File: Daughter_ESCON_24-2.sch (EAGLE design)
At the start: 29 parts

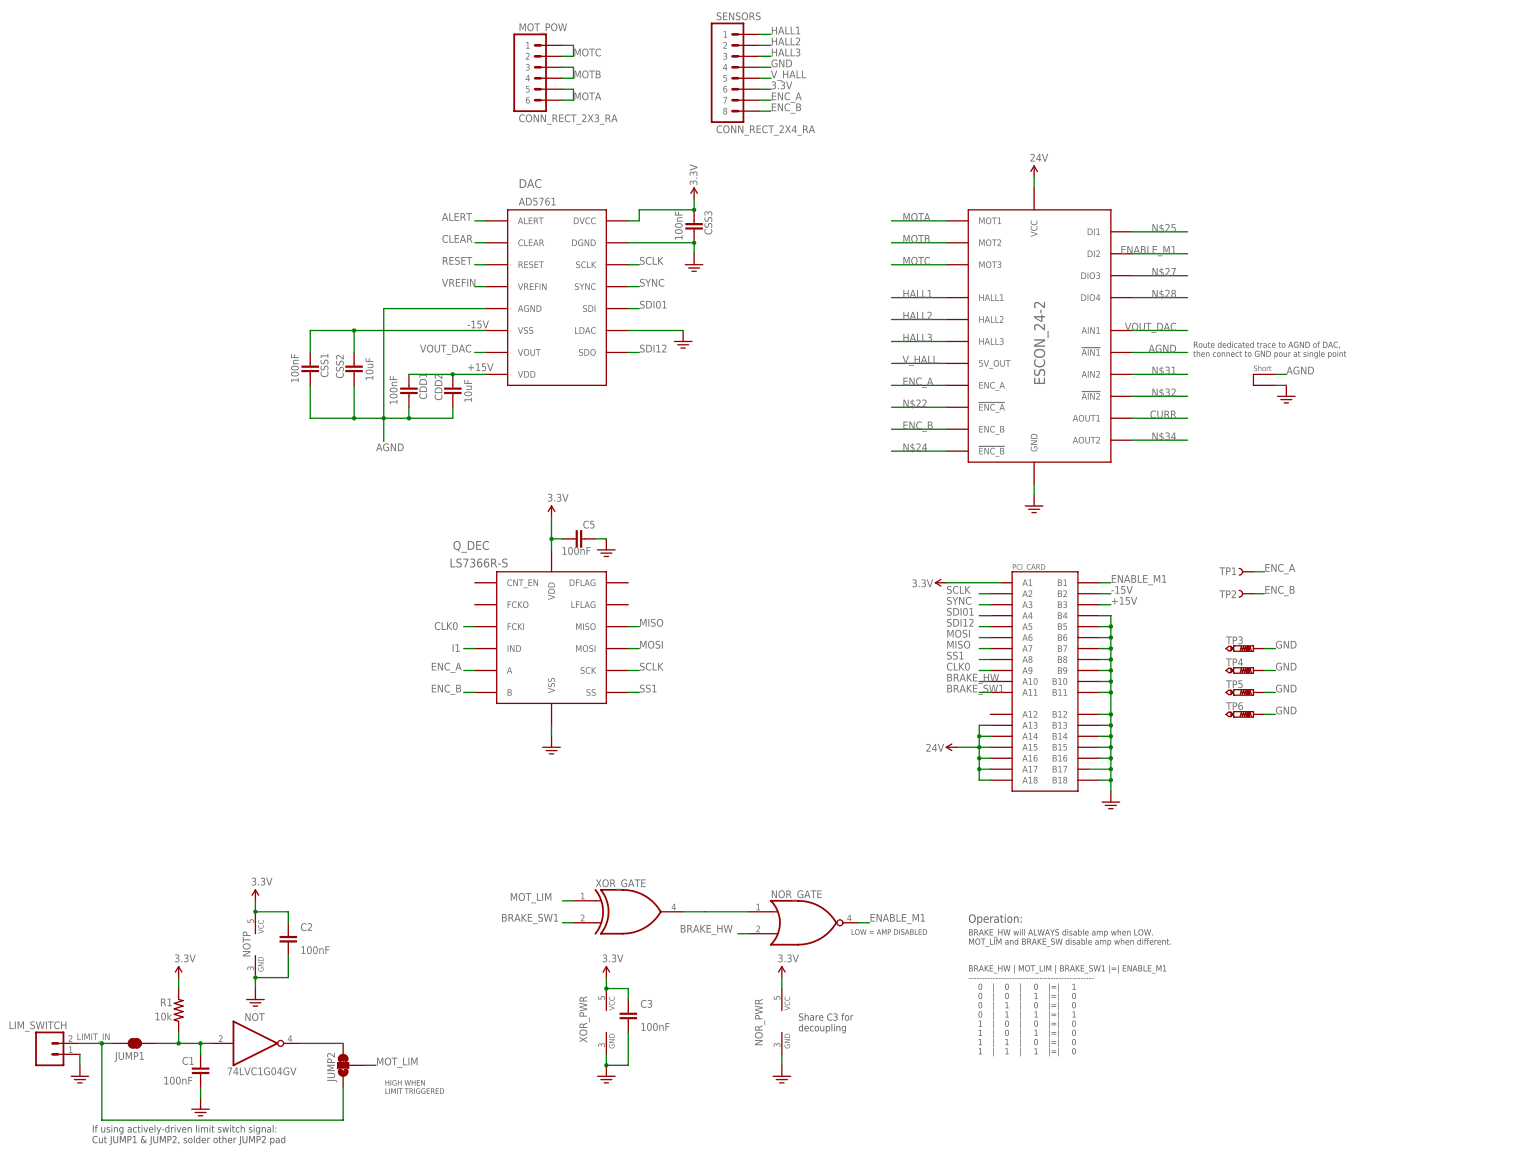
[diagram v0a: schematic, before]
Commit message: Protection circuitry added but not routed
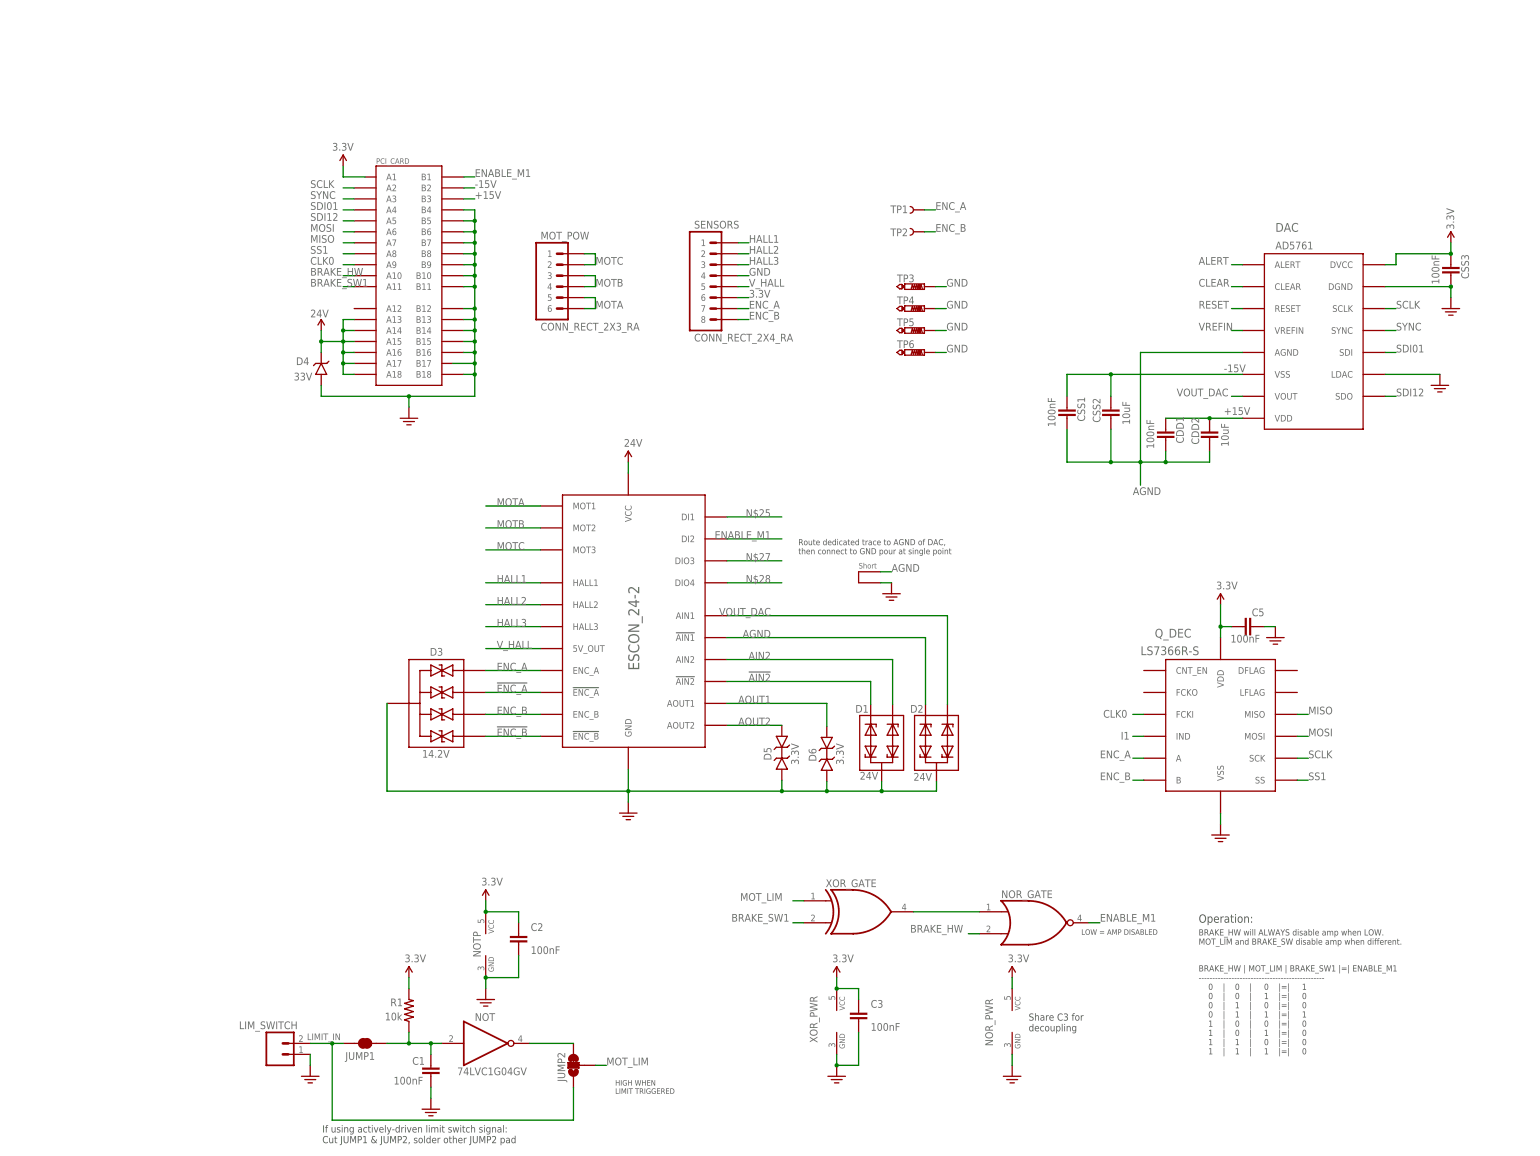
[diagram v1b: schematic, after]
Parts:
- added D1, D2: 24V, Cannula_1_0:DIODE_TVS_BIDIR_2
- added D3: 14.2V, Cannula_1_0:DIODE_TVS_BIDIR_4
- added D4: 33V, Cannula_1_0:DIODE_TVS_UNIDIR_1
- added D5, D6: 3.3V, Cannula_1_0:DIODE_TVS_BIDIR_1
- ESCON_24-2: value ESCON_MODULE_24-2 -> ESCON_MODULE24-2_BOTTOM_ENTRY; device Cannula_1_0:ESCON_MODULE_24-2 -> Cannula_1_0:ESCON_MODULE24-2_BOTTOM_ENTRY
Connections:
- removed net CURR: ESCON_24-2.AOUT1
- removed net N$22: ESCON_24-2.!ENC_A
- removed net N$24: ESCON_24-2.!ENC_B
- removed net N$31: ESCON_24-2.AIN2
- removed net N$32: ESCON_24-2.!AIN2
- removed net N$34: ESCON_24-2.AOUT2
- new net !AIN2: D1.2, ESCON_24-2.!AIN2
- new net !ENC_A: D3.IO2, ESCON_24-2.!ENC_A
- new net !ENC_B: D3.IO4, ESCON_24-2.!ENC_B
- new net AIN2: D1.1, ESCON_24-2.AIN2
- new net AOUT1: D6.A, ESCON_24-2.AOUT1
- new net AOUT2: D5.A, ESCON_24-2.AOUT2
- net 24V: now also D4.C
- net AGND: now also D2.2
- net ENC_A: now also D3.IO1
- net ENC_B: now also D3.IO3
- net GND: now also D1.3, D2.3, D3.GND, D4.A, D5.C, D6.C
- net VOUT_DAC: now also D2.1
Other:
- moved on the sheet: C1, C2, C3, C5, CDD1, CDD2, CSS1, CSS2, CSS3, DAC, ESCON_24-2, JUMP1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

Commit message: Finished and generated gerbers
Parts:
- D1: value 24V -> 33V; device Cannula_1_0:DIODE_TVS_BIDIR_2 -> Cannula_1_0:DIODE_TVS_UNIDIR_1
- D2: value 24V -> 14.2V; device Cannula_1_0:DIODE_TVS_BIDIR_2 -> Cannula_1_0:DIODE_TVS_BIDIR_4
- D3: value 14.2V -> 3.3V; device Cannula_1_0:DIODE_TVS_BIDIR_4 -> Cannula_1_0:DIODE_TVS_BIDIR_1
- D4: value 33V -> 3.3V; device Cannula_1_0:DIODE_TVS_UNIDIR_1 -> Cannula_1_0:DIODE_TVS_BIDIR_1
- D5, D6: value 3.3V -> 24V; device Cannula_1_0:DIODE_TVS_BIDIR_1 -> Cannula_1_0:DIODE_TVS_BIDIR_2
- renumbered C5 to C4, JUMP1 to JP1, JUMP2 to JP2
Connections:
- net !AIN2: now also D5.2; no longer D1.2
- net !ENC_A: now also D2.IO2; no longer D3.IO2
- net !ENC_B: now also D2.IO3; no longer D3.IO4
- net 24V: now also D1.C; no longer D4.C
- net AGND: now also D6.2; no longer D2.2
- net AIN2: now also D5.1; no longer D1.1
- net AOUT1: now also D4.A; no longer D6.A
- net AOUT2: now also D3.A; no longer D5.A
- net ENC_A: now also D2.IO1; no longer D3.IO1
- net ENC_B: now also D2.IO4; no longer D3.IO3
- net GND: now also D1.A, D2.GND, D3.C, D4.C, D5.3, D6.3; no longer D1.3, D2.3, D3.GND, D4.A, D5.C, D6.C
- net VOUT_DAC: now also D6.1; no longer D2.1

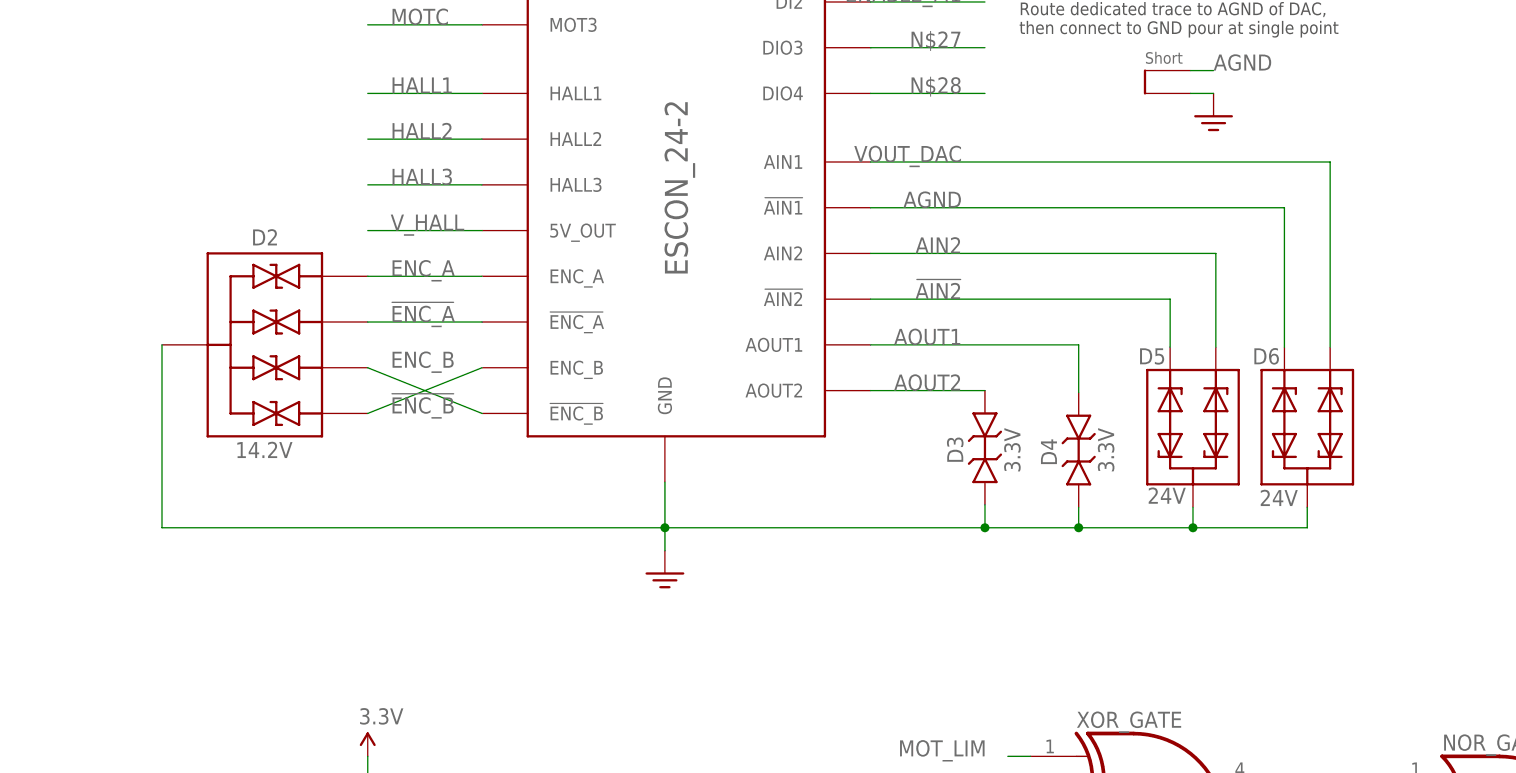
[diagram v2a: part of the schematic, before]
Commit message: Replaced 3.3V TVS with larger package
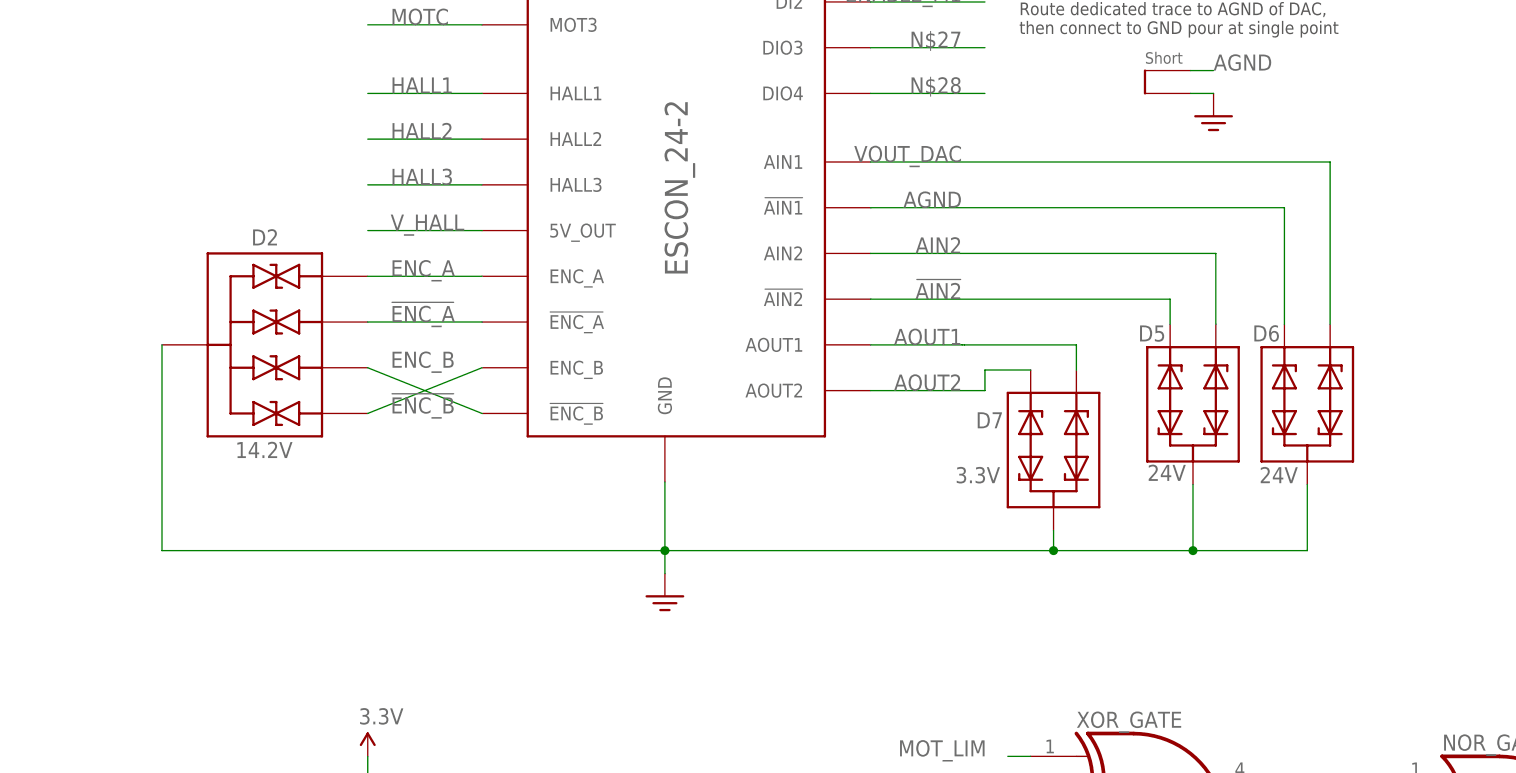
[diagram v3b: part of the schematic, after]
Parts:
- removed D3, D4: 3.3V, Cannula_1_0:DIODE_TVS_BIDIR_1
- added D7: 3.3V, Cannula_1_0:DIODE_TVS_BIDIR_2
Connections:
- net AOUT1: now also D7.1; no longer D4.A
- net AOUT2: now also D7.2; no longer D3.A
- net GND: now also D7.3; no longer D3.C, D4.C
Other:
- moved on the sheet: D5, D6
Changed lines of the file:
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@@
 <?xml version="1.0" encoding="utf-8"?>
 <!DOCTYPE eagle SYSTEM "eagle.dtd">
-<eagle version="9.2.2">
+<eagle version="9.3.1">
 <drawing>
 <settings>
@@
 <part name="D5" library="Cannula_1_0" deviceset="DIODE_TVS_BIDIR_2" device="" package3d_urn="urn:adsk.eagle:package:6452074/1" value="24V"/>
 <part name="D1" library="Cannula_1_0" deviceset="DIODE_TVS_UNIDIR_1" device="" package3d_urn="urn:adsk.eagle:package:43433/2" value="33V"/>
-<part name="D4" library="Cannula_1_0" deviceset="DIODE_TVS_BIDIR_1" device="" package3d_urn="urn:adsk.eagle:package:6452786/1" value="3.3V"/>
-<part name="D3" library="Cannula_1_0" deviceset="DIODE_TVS_BIDIR_1" device="" package3d_urn="urn:adsk.eagle:package:6452786/1" value="3.3V"/>
+<part name="D7" library="Cannula_1_0" deviceset="DIODE_TVS_BIDIR_2" device="" package3d_urn="urn:adsk.eagle:package:6452074/1" value="3.3V"/>
 </parts>
 <sheets>
@@
 <attribute name="NAME" x="-45.72" y="-5.08" size="2.54" layer="95" ratio="10" rot="R90"/>
 </instance>
-<instance part="GND4" gate="G$1" x="-48.26" y="-38.1" smashed="yes"/>
+<instance part="GND4" gate="G$1" x="-48.26" y="-40.64" smashed="yes"/>
 <instance part="SUPPLY6" gate="G$1" x="-48.26" y="43.18" smashed="yes">
 <attribute name="VALUE" x="-49.276" y="46.736" size="1.778" layer="96"/>
@@
 <attribute name="VALUE" x="-96.012" y="-23.495" size="1.778" layer="96" rot="MR180"/>
 </instance>
-<instance part="D6" gate="G$1" x="23.114" y="-20.574" smashed="yes" rot="R270">
-<attribute name="NAME" x="17.018" y="-14.859" size="1.778" layer="95"/>
-<attribute name="VALUE" x="17.78" y="-30.607" size="1.778" layer="96"/>
-</instance>
-<instance part="D5" gate="G$1" x="10.414" y="-20.574" smashed="yes" rot="R270">
-<attribute name="NAME" x="4.318" y="-14.859" size="1.778" layer="95"/>
-<attribute name="VALUE" x="5.334" y="-30.353" size="1.778" layer="96"/>
+<instance part="D6" gate="G$1" x="23.114" y="-18.034" smashed="yes" rot="R270">
+<attribute name="NAME" x="17.018" y="-12.319" size="1.778" layer="95"/>
+<attribute name="VALUE" x="17.78" y="-28.067" size="1.778" layer="96"/>
+</instance>
+<instance part="D5" gate="G$1" x="10.414" y="-18.034" smashed="yes" rot="R270">
+<attribute name="NAME" x="4.318" y="-12.319" size="1.778" layer="95"/>
+<attribute name="VALUE" x="5.334" y="-27.813" size="1.778" layer="96"/>
 </instance>
 <instance part="D1" gate="G$1" x="-119.38" y="66.04" smashed="yes" rot="R270">
@@
 <attribute name="VALUE" x="-125.73" y="62.103" size="1.778" layer="96"/>
 </instance>
-<instance part="D4" gate="G$1" x="-2.286" y="-25.654" smashed="yes" rot="R90">
-<attribute name="NAME" x="-4.699" y="-26.162" size="1.778" layer="95" rot="R90"/>
-<attribute name="VALUE" x="1.651" y="-26.924" size="1.778" layer="96" rot="R90"/>
-</instance>
-<instance part="D3" gate="G$1" x="-12.7" y="-25.4" smashed="yes" rot="R90">
-<attribute name="NAME" x="-15.113" y="-25.908" size="1.778" layer="95" rot="R90"/>
-<attribute name="VALUE" x="-8.763" y="-26.924" size="1.778" layer="96" rot="R90"/>
+<instance part="D7" gate="G$1" x="-5.08" y="-23.114" smashed="yes" rot="R270">
+<attribute name="NAME" x="-13.716" y="-21.971" size="1.778" layer="95"/>
+<attribute name="VALUE" x="-16.002" y="-28.067" size="1.778" layer="96"/>
 </instance>
 </instances>
@@
 <segment>
 <pinref part="ESCON_24-2" gate="G$1" pin="GND"/>
-<wire x1="-48.26" y1="-27.94" x2="-48.26" y2="-33.02" width="0.1524" layer="91"/>
+<wire x1="-48.26" y1="-27.94" x2="-48.26" y2="-35.56" width="0.1524" layer="91"/>
 <pinref part="GND4" gate="G$1" pin="GND"/>
 <pinref part="D6" gate="G$1" pin="3"/>
-<wire x1="-48.26" y1="-33.02" x2="-48.26" y2="-35.56" width="0.1524" layer="91"/>
-<wire x1="23.114" y1="-30.734" x2="23.114" y2="-33.02" width="0.1524" layer="91"/>
-<wire x1="23.114" y1="-33.02" x2="10.414" y2="-33.02" width="0.1524" layer="91"/>
+<wire x1="-48.26" y1="-35.56" x2="-48.26" y2="-38.1" width="0.1524" layer="91"/>
+<wire x1="23.114" y1="-28.194" x2="23.114" y2="-35.56" width="0.1524" layer="91"/>
+<wire x1="23.114" y1="-35.56" x2="10.414" y2="-35.56" width="0.1524" layer="91"/>
 <pinref part="D5" gate="G$1" pin="3"/>
-<wire x1="10.414" y1="-33.02" x2="-2.286" y2="-33.02" width="0.1524" layer="91"/>
-<wire x1="-2.286" y1="-33.02" x2="-12.7" y2="-33.02" width="0.1524" layer="91"/>
-<wire x1="10.414" y1="-30.734" x2="10.414" y2="-33.02" width="0.1524" layer="91"/>
-<junction x="10.414" y="-33.02"/>
-<pinref part="D4" gate="G$1" pin="C"/>
-<wire x1="-2.286" y1="-30.734" x2="-2.286" y2="-33.02" width="0.1524" layer="91"/>
-<junction x="-2.286" y="-33.02"/>
-<pinref part="D3" gate="G$1" pin="C"/>
-<wire x1="-12.7" y1="-30.48" x2="-12.7" y2="-33.02" width="0.1524" layer="91"/>
-<wire x1="-12.7" y1="-33.02" x2="-48.26" y2="-33.02" width="0.1524" layer="91"/>
-<junction x="-12.7" y="-33.02"/>
-<junction x="-48.26" y="-33.02"/>
+<wire x1="10.414" y1="-28.194" x2="10.414" y2="-35.56" width="0.1524" layer="91"/>
+<junction x="10.414" y="-35.56"/>
+<wire x1="10.414" y1="-35.56" x2="-5.08" y2="-35.56" width="0.1524" layer="91"/>
+<junction x="-48.26" y="-35.56"/>
 <pinref part="D2" gate="G$1" pin="GND"/>
-<wire x1="-104.14" y1="-12.7" x2="-104.14" y2="-33.02" width="0.1524" layer="91"/>
-<wire x1="-104.14" y1="-33.02" x2="-48.26" y2="-33.02" width="0.1524" layer="91"/>
+<wire x1="-5.08" y1="-35.56" x2="-48.26" y2="-35.56" width="0.1524" layer="91"/>
+<wire x1="-104.14" y1="-12.7" x2="-104.14" y2="-35.56" width="0.1524" layer="91"/>
+<wire x1="-104.14" y1="-35.56" x2="-48.26" y2="-35.56" width="0.1524" layer="91"/>
+<pinref part="D7" gate="G$1" pin="3"/>
+<wire x1="-5.08" y1="-33.274" x2="-5.08" y2="-35.56" width="0.1524" layer="91"/>
+<junction x="-5.08" y="-35.56"/>
 </segment>
 <segment>
@@
 <wire x1="25.654" y1="7.62" x2="-25.4" y2="7.62" width="0.1524" layer="91"/>
 <pinref part="D6" gate="G$1" pin="1"/>
-<wire x1="25.654" y1="-12.954" x2="25.654" y2="7.62" width="0.1524" layer="91"/>
+<wire x1="25.654" y1="-10.414" x2="25.654" y2="7.62" width="0.1524" layer="91"/>
 </segment>
 </net>
@@
 <segment>
 <pinref part="ESCON_24-2" gate="G$1" pin="AOUT1"/>
-<wire x1="-25.4" y1="-12.7" x2="-2.286" y2="-12.7" width="0.1524" layer="91"/>
+<wire x1="-25.4" y1="-12.7" x2="-15.24" y2="-12.7" width="0.1524" layer="91"/>
 <label x="-15.24" y="-12.7" size="1.778" layer="95" align="bottom-right"/>
-<pinref part="D4" gate="G$1" pin="A"/>
-<wire x1="-2.286" y1="-18.034" x2="-2.286" y2="-12.7" width="0.1524" layer="91"/>
+<pinref part="D7" gate="G$1" pin="1"/>
+<wire x1="-15.24" y1="-12.7" x2="-14.986" y2="-12.7" width="0.1524" layer="91"/>
+<wire x1="-2.54" y1="-15.494" x2="-2.54" y2="-12.7" width="0.1524" layer="91"/>
+<wire x1="-2.54" y1="-12.7" x2="-14.986" y2="-12.7" width="0.1524" layer="91"/>
 </segment>
 </net>
@@
 <wire x1="12.954" y1="-2.54" x2="-25.4" y2="-2.54" width="0.1524" layer="91"/>
 <pinref part="D5" gate="G$1" pin="1"/>
-<wire x1="12.954" y1="-12.954" x2="12.954" y2="-2.54" width="0.1524" layer="91"/>
+<wire x1="12.954" y1="-10.414" x2="12.954" y2="-2.54" width="0.1524" layer="91"/>
 </segment>
 </net>
@@
 <wire x1="7.874" y1="-7.62" x2="-25.4" y2="-7.62" width="0.1524" layer="91"/>
 <pinref part="D5" gate="G$1" pin="2"/>
-<wire x1="7.874" y1="-12.954" x2="7.874" y2="-7.62" width="0.1524" layer="91"/>
+<wire x1="7.874" y1="-10.414" x2="7.874" y2="-7.62" width="0.1524" layer="91"/>
 </segment>
 </net>
@@
 <wire x1="-25.4" y1="-17.78" x2="-12.7" y2="-17.78" width="0.1524" layer="91"/>
 <label x="-15.24" y="-17.78" size="1.778" layer="95" align="bottom-right"/>
-<pinref part="D3" gate="G$1" pin="A"/>
+<pinref part="D7" gate="G$1" pin="2"/>
+<wire x1="-7.62" y1="-15.494" x2="-12.7" y2="-15.494" width="0.1524" layer="91"/>
+<wire x1="-12.7" y1="-15.494" x2="-12.7" y2="-17.78" width="0.1524" layer="91"/>
 </segment>
 </net>
@@
 <wire x1="20.574" y1="2.54" x2="-25.4" y2="2.54" width="0.1524" layer="91"/>
 <pinref part="D6" gate="G$1" pin="2"/>
-<wire x1="20.574" y1="-12.954" x2="20.574" y2="2.54" width="0.1524" layer="91"/>
-</segment>
-<segment>
+<wire x1="20.574" y1="-10.414" x2="20.574" y2="2.54" width="0.1524" layer="91"/>
+</segment>
+<segment>
